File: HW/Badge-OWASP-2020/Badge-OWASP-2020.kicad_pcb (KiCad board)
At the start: 2 copper layers, 25 parts, among them J1 Conn_02x03_Odd_Even, J2 Screw_Terminal_01x04, J3 USB_B, Q1 MMBT3904, Q2 MMBT3904, SW1 RST, SW2 BOOT, U1 ESP32-WROOM-32, U2 CH340C, U3 AP111733

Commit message: define design :D
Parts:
- added J2: Battery, Connector_PinHeader_2.54mm:PinHeader_1x02_P2.54mm_Vertical, F.Cu at (163.3, 89.2)
- added Q2: DMG3415U-7, Package_TO_SOT_SMD:SOT-23, B.Cu at (147.6, 61.2)
- added R7: 100K, Resistor_SMD:R_0805_2012Metric_Pad1.15x1.40mm_HandSolder, B.Cu at (147.8, 56.9)
- added Ref**: Val**, Aesthetics:Badge_2020_OWASP, F.Cu at (147.1, 66.0)
- C1, C2, C3, C4, C5, D1, D2, D3, F1, Q1, R1, R2, R3, R4, R5, R6, U1, U2: moved to B.Cu
- J1: value Conn_02x03_Odd_Even -> Shitty Add-Ons; moved to B.Cu
- J3: renamed from J2; value Screw_Terminal_01x04 -> I2C
- J4: renamed from J3; moved to B.Cu
- Q3: renamed from Q2; moved to B.Cu
- U3: value AP111733 -> AP1117; moved to B.Cu
- moved D1 91.4 mm to (118.6, 71.1)
- moved R1 85.3 mm to (113.0, 51.3)
- moved C1 84.2 mm to (113.0, 47.2)
- moved D2 82.8 mm to (127.5, 81.8)
- moved J3 80.0 mm to (104.6, 36.3)
- moved R6 76.5 mm to (123.1, 57.2)
- moved Q3 74.2 mm to (127.7, 59.4)
- moved R2 73.4 mm to (123.1, 60.2)
- moved R5 69.6 mm to (130.1, 64.3)
- moved C3 67.7 mm to (140.8, 54.0)
- moved C4 67.7 mm to (140.0, 57.4)
- moved D3 67.7 mm to (135.7, 54.2)
- moved R4 67.7 mm to (140.0, 60.3)
- moved R3 67.4 mm to (130.1, 67.2)
- moved Q1 66.1 mm to (138.3, 69.4)
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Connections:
- D2 pad 2: Net-(D2-Pad2) -> /GPIO1
- J1 pad 1: GND -> +3V3
- J1 pad 2: +3V3 -> GND
- J1 pad 3: /SCL -> /SDA
- J1 pad 4: /SDA -> /SCL
- J1 pad 5: /GPIO2 -> /GPIO1
- J1 pad 6: /GPIO1 -> /GPIO2
- U1 pad 24: /GPIO1 -> Net-(U1-Pad24)
- U2 pad 2: /TXD -> /TX
- U2 pad 3: /RXD -> /RX
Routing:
- added copper zone on F.Cu, net GND
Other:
- board outline added: 98.6 x 65.9 mm

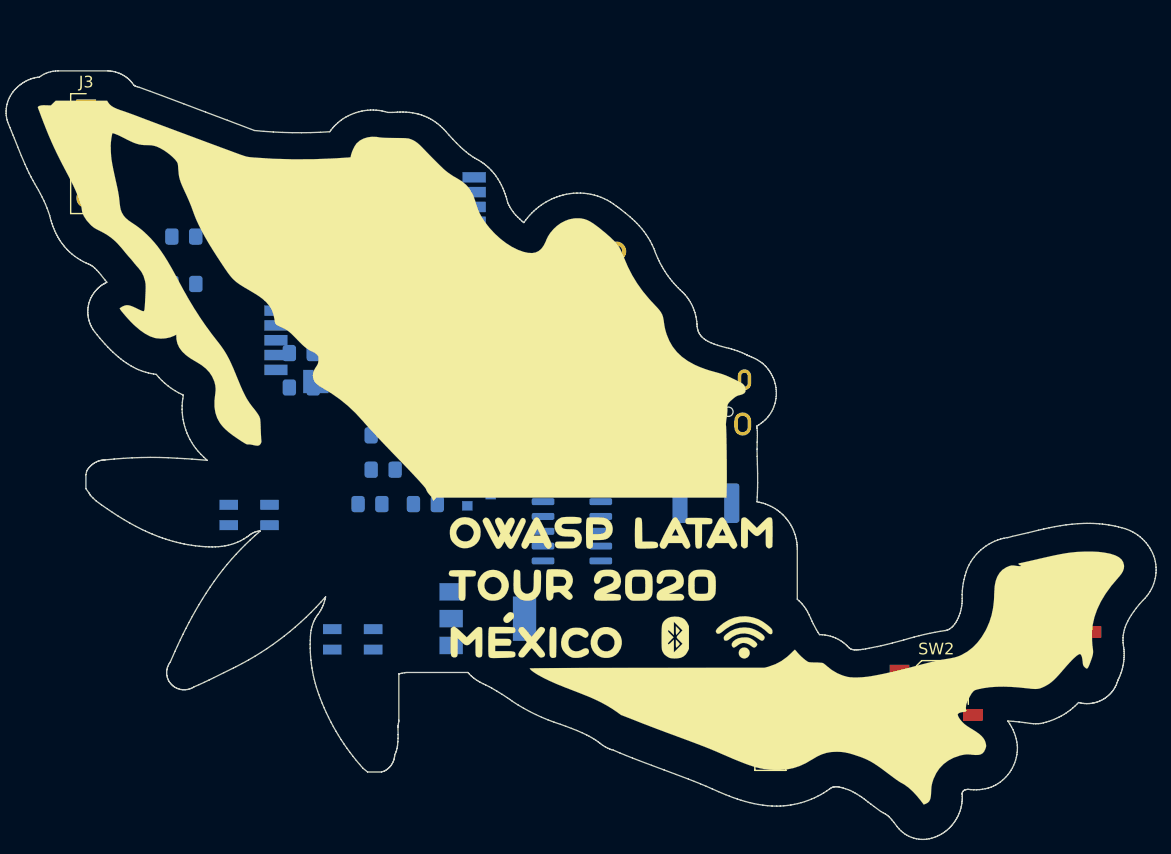
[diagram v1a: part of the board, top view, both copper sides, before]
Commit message: component distribution
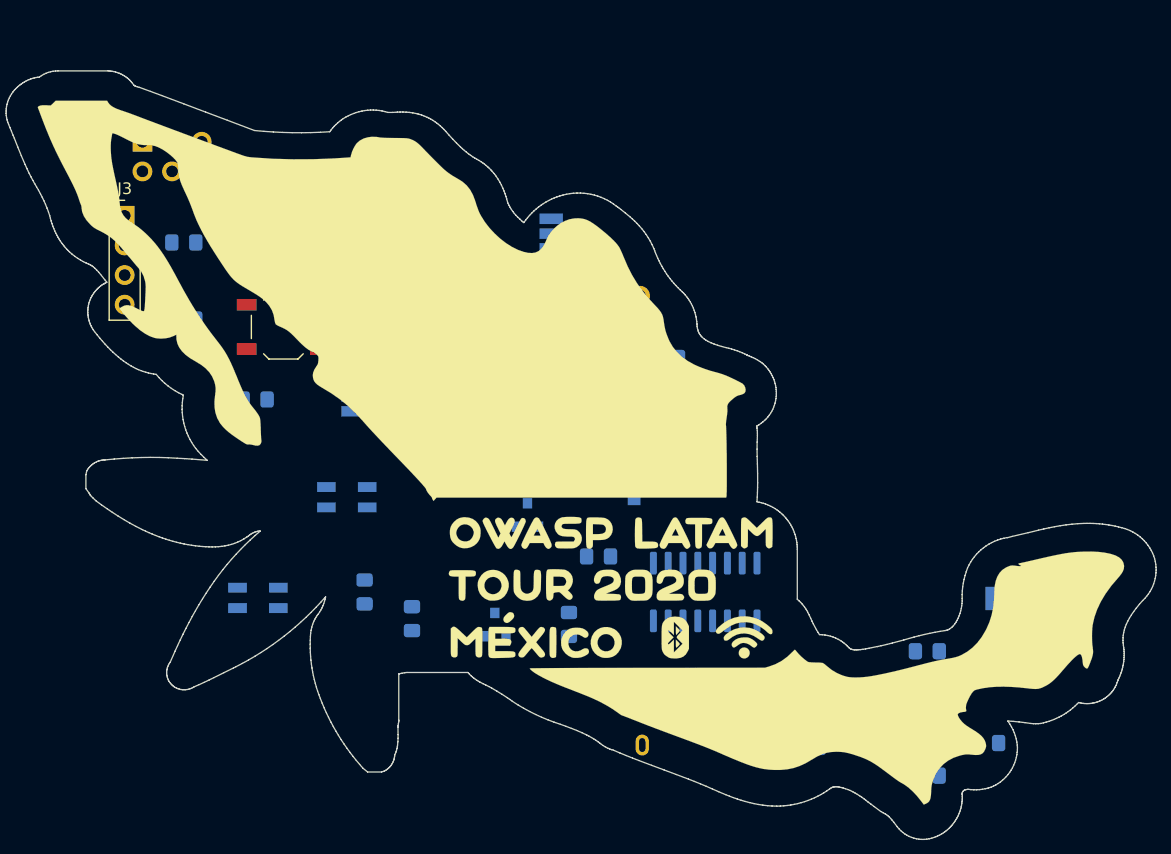
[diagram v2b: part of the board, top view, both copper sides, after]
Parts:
- J2: moved to B.Cu
- moved SW1 70.4 mm to (121.6, 55.0)
- moved SW2 68.1 mm to (121.5, 47.6)
- moved C4 53.5 mm to (181.9, 90.7)
- moved R7 46.6 mm to (176.8, 93.5)
- moved C5 44.9 mm to (176.8, 82.8)
- moved U3 44.6 mm to (183.7, 81.4), turned to 90 degrees
- moved R1 43.0 mm to (154.7, 62.0)
- moved C1 42.7 mm to (154.4, 57.7)
- moved J1 42.4 mm to (109.5, 39.1), turned to 270 degrees
- moved Q2 40.1 mm to (176.8, 88.6)
- moved J2 39.3 mm to (149.6, 52.3), turned to 270 degrees
- moved R6 32.7 mm to (146.1, 80.5), turned to 90 degrees
- moved R4 29.8 mm to (113.0, 47.8), turned to 180 degrees
- moved R2 29.3 mm to (148.6, 74.7)
- moved J4 27.5 mm to (156.2, 88.9), turned to 180 degrees
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
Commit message: countour circle
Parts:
- moved J2 37.9 mm to (168.1, 85.3)
- moved SW1 36.8 mm to (157.1, 64.4)
- moved SW2 30.2 mm to (146.7, 64.4)
- moved Q3 6.01 mm to (143.6, 85.1)
- moved R6 5.79 mm to (149.6, 85.1)
- moved F1 2.64 mm to (164.8, 91.0)
- moved U2 1.44 mm to (158.8, 78.7)
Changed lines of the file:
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@@
   (general
     (thickness 1.6)
-    (drawings 2)
+    (drawings 5)
     (tracks 0)
     (zones 0)
@@
   (page A4)
   (layers
-    (0 F.Cu signal)
-    (31 B.Cu signal)
+    (0 F.Cu signal hide)
+    (31 B.Cu signal hide)
     (32 B.Adhes user)
     (33 F.Adhes user)
     (34 B.Paste user)
     (35 F.Paste user)
-    (36 B.SilkS user)
+    (36 B.SilkS user hide)
     (37 F.SilkS user hide)
     (38 B.Mask user)
@@
   )
   (module Connector_PinHeader_2.54mm:PinHeader_1x02_P2.54mm_Vertical (layer B.Cu)
-    (at 149.606 52.324 270)
+    (at 168.148 85.344 270)
     (descr "Through hole straight pin header, 1x02, 2.54mm pitch, single row")
     (tags "Through hole pin header THT 1x02 2.54mm single row")
@@
   )
   (module Package_SO:SOIC-16_3.9x9.9mm_P1.27mm (layer B.Cu)
-    (at 157.734 77.724 90)
+    (at 158.75 78.74 90)
     (descr "SOIC, 16 Pin (JEDEC MS-012AC, https://www.analog.com/media/en/package-pcb-resources/package/pkg_pdf/soic_narrow-r/r_16.pdf), generated with kicad-footprint-generator ipc_gullwing_generator.py")
     (tags "SOIC SO")
@@
   )
   (module Button_Switch_SMD:SW_SPST_TL3342 (layer F.Cu)
-    (at 121.514 47.62)
+    (at 146.66 64.394)
     (descr "Low-profile SMD Tactile Switch, https://www.e-switch.com/system/asset/product_line/data_sheet/165/TL3342.pdf")
     (tags "SPST Tactile Switch")
@@
   )
   (module Button_Switch_SMD:SW_SPST_TL3342 (layer F.Cu)
-    (at 121.564 54.996)
+    (at 157.124 64.394)
     (descr "Low-profile SMD Tactile Switch, https://www.e-switch.com/system/asset/product_line/data_sheet/165/TL3342.pdf")
     (tags "SPST Tactile Switch")
@@
   )
   (module Resistor_SMD:R_0805_2012Metric_Pad1.15x1.40mm_HandSolder (layer B.Cu)
-    (at 146.05 80.509 90)
+    (at 149.606 85.081 90)
     (descr "Resistor SMD 0805 (2012 Metric), square (rectangular) end terminal, IPC_7351 nominal with elongated pad for handsoldering. (Body size source: https://docs.google.com/spreadsheets/d/1BsfQQcO9C6DZCsRaXUlFlo91Tg2WpOkGARC1WS5S8t0/edit?usp=sharing), generated with kicad-footprint-generator")
     (tags "resistor handsolder")
@@
   )
   (module Package_TO_SOT_SMD:SOT-23 (layer B.Cu)
-    (at 139.7 80.518 90)
+    (at 143.576 85.106 90)
     (descr "SOT-23, Standard")
     (tags SOT-23)
@@
   )
   (module Fuse:Fuse_1812_4532Metric_Pad1.30x3.40mm_HandSolder (layer B.Cu)
-    (at 166.37 88.839 90)
+    (at 164.846 90.993 90)
     (descr "Fuse SMD 1812 (4532 Metric), square (rectangular) end terminal, IPC_7351 nominal with elongated pad for handsoldering. (Body size source: https://www.nikhef.nl/pub/departments/mt/projects/detectorR_D/dtddice/ERJ2G.pdf), generated with kicad-footprint-generator")
     (tags "resistor handsolder")
@@
     )
   )
+  (gr_circle (center 103.124 37.989769) (end 105.156 36.719769) (layer Edge.Cuts) (width 0.05))
+  (dimension 4.792462 (width 0.15) (layer Dwgs.User)
+    (gr_text "4.792 mm" (at 198.912 76.343769 270) (layer Dwgs.User)
+      (effects (font (size 1 1) (thickness 0.15)))
+    )
+    (feature1 (pts (xy 191.77 78.74) (xy 198.198421 78.74)))
+    (feature2 (pts (xy 191.77 73.947538) (xy 198.198421 73.947538)))
+    (crossbar (pts (xy 197.612 73.947538) (xy 197.612 78.74)))
+    (arrow1a (pts (xy 197.612 78.74) (xy 197.025579 77.613496)))
+    (arrow1b (pts (xy 197.612 78.74) (xy 198.198421 77.613496)))
+    (arrow2a (pts (xy 197.612 73.947538) (xy 197.025579 75.074042)))
+    (arrow2b (pts (xy 197.612 73.947538) (xy 198.198421 75.074042)))
+  )
+  (gr_circle (center 191.77 76.343769) (end 193.802 75.073769) (layer Edge.Cuts) (width 0.05))
   (dimension 99.080164 (width 0.15) (layer Margin)
     (gr_text "99.080 mm" (at 148.26013 123.912709 0.1040899169) (layer Margin)

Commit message: logos space
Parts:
- moved C3 21.9 mm to (115.3, 82.8)
- moved R5 12.0 mm to (144.5, 80.8), turned to 0 degrees
- moved D3 6.55 mm to (157.9, 70.4), turned to 180 degrees
- moved Q1 5.18 mm to (144.3, 76.0)
- moved R2 4.75 mm to (149.9, 79.2), turned to 90 degrees
- moved R1 4.69 mm to (157.7, 65.5)
- moved C1 4.13 mm to (157.5, 60.5)
- moved C2 3.64 mm to (127.8, 74.2), turned to 0 degrees
- moved D2 0.84 mm to (119.9, 77.6)
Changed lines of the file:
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@@
   (page A4)
   (layers
-    (0 F.Cu signal hide)
-    (31 B.Cu signal hide)
+    (0 F.Cu signal)
+    (31 B.Cu signal)
     (32 B.Adhes user)
     (33 F.Adhes user)
     (34 B.Paste user)
     (35 F.Paste user)
-    (36 B.SilkS user hide)
+    (36 B.SilkS user)
     (37 F.SilkS user hide)
     (38 B.Mask user)
@@
   )
   (module Resistor_SMD:R_0805_2012Metric_Pad1.15x1.40mm_HandSolder (layer B.Cu)
-    (at 132.588 80.01 270)
+    (at 144.526 80.772)
     (descr "Resistor SMD 0805 (2012 Metric), square (rectangular) end terminal, IPC_7351 nominal with elongated pad for handsoldering. (Body size source: https://docs.google.com/spreadsheets/d/1BsfQQcO9C6DZCsRaXUlFlo91Tg2WpOkGARC1WS5S8t0/edit?usp=sharing), generated with kicad-footprint-generator")
     (tags "resistor handsolder")
     (attr smd)
-    (fp_text reference R5 (at 0 1.65 90) (layer B.SilkS)
+    (fp_text reference R5 (at 0 1.65) (layer B.SilkS)
       (effects (font (size 1 1) (thickness 0.15)) (justify mirror))
     )
-    (fp_text value 10K (at 0 -1.65 90) (layer B.Fab)
+    (fp_text value 10K (at 0 -1.65) (layer B.Fab)
       (effects (font (size 1 1) (thickness 0.15)) (justify mirror))
     )
-    (fp_text user %R (at 0 0 90) (layer B.Fab)
+    (fp_text user %R (at 0 0) (layer B.Fab)
       (effects (font (size 0.5 0.5) (thickness 0.08)) (justify mirror))
     )
@@
     (fp_line (start -1 0.6) (end 1 0.6) (layer B.Fab) (width 0.1))
     (fp_line (start -1 -0.6) (end -1 0.6) (layer B.Fab) (width 0.1))
-    (pad 2 smd roundrect (at 1.025 0 270) (size 1.15 1.4) (layers B.Cu B.Paste B.Mask) (roundrect_rratio 0.217391)
+    (pad 2 smd roundrect (at 1.025 0) (size 1.15 1.4) (layers B.Cu B.Paste B.Mask) (roundrect_rratio 0.217391)
       (net 17 /DTR))
-    (pad 1 smd roundrect (at -1.025 0 270) (size 1.15 1.4) (layers B.Cu B.Paste B.Mask) (roundrect_rratio 0.217391)
+    (pad 1 smd roundrect (at -1.025 0) (size 1.15 1.4) (layers B.Cu B.Paste B.Mask) (roundrect_rratio 0.217391)
       (net 16 "Net-(Q1-Pad1)"))
     (model ${KISYS3DMOD}/Resistor_SMD.3dshapes/R_0805_2012Metric.wrl
@@
   )
   (module Resistor_SMD:R_0805_2012Metric_Pad1.15x1.40mm_HandSolder (layer B.Cu)
-    (at 148.59 74.676)
+    (at 149.86 79.248 90)
     (descr "Resistor SMD 0805 (2012 Metric), square (rectangular) end terminal, IPC_7351 nominal with elongated pad for handsoldering. (Body size source: https://docs.google.com/spreadsheets/d/1BsfQQcO9C6DZCsRaXUlFlo91Tg2WpOkGARC1WS5S8t0/edit?usp=sharing), generated with kicad-footprint-generator")
     (tags "resistor handsolder")
     (attr smd)
-    (fp_text reference R2 (at 0 1.65) (layer B.SilkS)
+    (fp_text reference R2 (at 0 1.65 90) (layer B.SilkS)
       (effects (font (size 1 1) (thickness 0.15)) (justify mirror))
     )
-    (fp_text value 470 (at 0 -1.65) (layer B.Fab)
+    (fp_text value 470 (at 0 -1.65 90) (layer B.Fab)
       (effects (font (size 1 1) (thickness 0.15)) (justify mirror))
     )
-    (fp_text user %R (at 0 0) (layer B.Fab)
+    (fp_text user %R (at 0 0 90) (layer B.Fab)
       (effects (font (size 0.5 0.5) (thickness 0.08)) (justify mirror))
     )
@@
     (fp_line (start -1 0.6) (end 1 0.6) (layer B.Fab) (width 0.1))
     (fp_line (start -1 -0.6) (end -1 0.6) (layer B.Fab) (width 0.1))
-    (pad 2 smd roundrect (at 1.025 0) (size 1.15 1.4) (layers B.Cu B.Paste B.Mask) (roundrect_rratio 0.217391)
+    (pad 2 smd roundrect (at 1.025 0 90) (size 1.15 1.4) (layers B.Cu B.Paste B.Mask) (roundrect_rratio 0.217391)
       (net 19 "Net-(R2-Pad2)"))
-    (pad 1 smd roundrect (at -1.025 0) (size 1.15 1.4) (layers B.Cu B.Paste B.Mask) (roundrect_rratio 0.217391)
+    (pad 1 smd roundrect (at -1.025 0 90) (size 1.15 1.4) (layers B.Cu B.Paste B.Mask) (roundrect_rratio 0.217391)
       (net 5 /NP))
     (model ${KISYS3DMOD}/Resistor_SMD.3dshapes/R_0805_2012Metric.wrl
@@
   )
   (module Resistor_SMD:R_0805_2012Metric_Pad1.15x1.40mm_HandSolder (layer B.Cu)
-    (at 154.677 61.976)
+    (at 157.734 65.532)
     (descr "Resistor SMD 0805 (2012 Metric), square (rectangular) end terminal, IPC_7351 nominal with elongated pad for handsoldering. (Body size source: https://docs.google.com/spreadsheets/d/1BsfQQcO9C6DZCsRaXUlFlo91Tg2WpOkGARC1WS5S8t0/edit?usp=sharing), generated with kicad-footprint-generator")
     (tags "resistor handsolder")
@@
   )
   (module Package_TO_SOT_SMD:SOT-23 (layer B.Cu)
-    (at 142.494 71.12 90)
+    (at 144.338 75.962 90)
     (descr "SOT-23, Standard")
     (tags SOT-23)
@@
   )
   (module Diode_SMD:D_SOD-123F (layer B.Cu)
-    (at 151.638 68.326 270)
+    (at 157.864 70.358 180)
     (descr D_SOD-123F)
     (tags D_SOD-123F)
     (attr smd)
-    (fp_text reference D3 (at -0.127 1.905 90) (layer B.SilkS)
+    (fp_text reference D3 (at -0.127 1.905) (layer B.SilkS)
       (effects (font (size 1 1) (thickness 0.15)) (justify mirror))
     )
-    (fp_text value MBR120 (at 0 -2.1 90) (layer B.Fab)
+    (fp_text value MBR120 (at 0 -2.1) (layer B.Fab)
       (effects (font (size 1 1) (thickness 0.15)) (justify mirror))
     )
@@
     (fp_line (start 0.25 0) (end 0.75 0) (layer B.Fab) (width 0.1))
     (fp_line (start -2.2 1) (end -2.2 -1) (layer B.SilkS) (width 0.12))
-    (fp_text user %R (at -0.127 1.905 90) (layer B.Fab)
+    (fp_text user %R (at -0.127 1.905) (layer B.Fab)
       (effects (font (size 1 1) (thickness 0.15)) (justify mirror))
     )
-    (pad 2 smd rect (at 1.4 0 270) (size 1.1 1.1) (layers B.Cu B.Paste B.Mask)
+    (pad 2 smd rect (at 1.4 0 180) (size 1.1 1.1) (layers B.Cu B.Paste B.Mask)
       (net 6 VCC))
-    (pad 1 smd rect (at -1.4 0 270) (size 1.1 1.1) (layers B.Cu B.Paste B.Mask)
+    (pad 1 smd rect (at -1.4 0 180) (size 1.1 1.1) (layers B.Cu B.Paste B.Mask)
       (net 3 "Net-(C5-Pad1)"))
     (model ${KISYS3DMOD}/Diode_SMD.3dshapes/D_SOD-123F.wrl
@@
   )
   (module LED_SMD:LED_SK6812MINI_PLCC4_3.5x3.5mm_P1.75mm (layer B.Cu)
-    (at 119.38 78.232)
+    (at 119.916 77.583)
     (descr https://cdn-shop.adafruit.com/product-files/2686/SK6812MINI_REV.01-1-2.pdf)
     (tags "LED RGB NeoPixel Mini")
@@
   )
   (module Capacitor_SMD:C_0805_2012Metric_Pad1.15x1.40mm_HandSolder (layer B.Cu)
-    (at 119.135 61.214)
+    (at 115.316 82.804)
     (descr "Capacitor SMD 0805 (2012 Metric), square (rectangular) end terminal, IPC_7351 nominal with elongated pad for handsoldering. (Body size source: https://docs.google.com/spreadsheets/d/1BsfQQcO9C6DZCsRaXUlFlo91Tg2WpOkGARC1WS5S8t0/edit?usp=sharing), generated with kicad-footprint-generator")
     (tags "capacitor handsolder")
@@
   )
   (module Capacitor_SMD:C_0805_2012Metric_Pad1.15x1.40mm_HandSolder (layer B.Cu)
-    (at 128.524 77.724 90)
+    (at 127.753 74.168)
     (descr "Capacitor SMD 0805 (2012 Metric), square (rectangular) end terminal, IPC_7351 nominal with elongated pad for handsoldering. (Body size source: https://docs.google.com/spreadsheets/d/1BsfQQcO9C6DZCsRaXUlFlo91Tg2WpOkGARC1WS5S8t0/edit?usp=sharing), generated with kicad-footprint-generator")
     (tags "capacitor handsolder")
     (attr smd)
-    (fp_text reference C2 (at 0 1.65 90) (layer B.SilkS)
+    (fp_text reference C2 (at 0 1.65) (layer B.SilkS)
       (effects (font (size 1 1) (thickness 0.15)) (justify mirror))
     )
-    (fp_text value 0.1uF (at 0 -1.65 90) (layer B.Fab)
+    (fp_text value 0.1uF (at 0 -1.65) (layer B.Fab)
       (effects (font (size 1 1) (thickness 0.15)) (justify mirror))
     )
-    (fp_text user %R (at 0 0 90) (layer B.Fab)
+    (fp_text user %R (at 0 0) (layer B.Fab)
       (effects (font (size 0.5 0.5) (thickness 0.08)) (justify mirror))
     )
@@
     (fp_line (start -1 0.6) (end 1 0.6) (layer B.Fab) (width 0.1))
     (fp_line (start -1 -0.6) (end -1 0.6) (layer B.Fab) (width 0.1))
-    (pad 2 smd roundrect (at 1.025 0 90) (size 1.15 1.4) (layers B.Cu B.Paste B.Mask) (roundrect_rratio 0.217391)
+    (pad 2 smd roundrect (at 1.025 0) (size 1.15 1.4) (layers B.Cu B.Paste B.Mask) (roundrect_rratio 0.217391)
       (net 1 GND))
-    (pad 1 smd roundrect (at -1.025 0 90) (size 1.15 1.4) (layers B.Cu B.Paste B.Mask) (roundrect_rratio 0.217391)
+    (pad 1 smd roundrect (at -1.025 0) (size 1.15 1.4) (layers B.Cu B.Paste B.Mask) (roundrect_rratio 0.217391)
       (net 2 +3V3))
     (model ${KISYS3DMOD}/Capacitor_SMD.3dshapes/C_0805_2012Metric.wrl
@@
   )
   (module Capacitor_SMD:C_0805_2012Metric_Pad1.15x1.40mm_HandSolder (layer B.Cu)
-    (at 154.423 57.658)
+    (at 157.471 60.452)
     (descr "Capacitor SMD 0805 (2012 Metric), square (rectangular) end terminal, IPC_7351 nominal with elongated pad for handsoldering. (Body size source: https://docs.google.com/spreadsheets/d/1BsfQQcO9C6DZCsRaXUlFlo91Tg2WpOkGARC1WS5S8t0/edit?usp=sharing), generated with kicad-footprint-generator")
     (tags "capacitor handsolder")

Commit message: add logos
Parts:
- added G***: LOGO, Aesthetics:espressif, B.Cu at (147.1, 73.4)
- added G***: LOGO, Aesthetics:lcsc, B.Cu at (159.5, 77.7)
- added G***: LOGO, Aesthetics:pcbway_13x4, B.Cu at (145.0, 81.8)
- added G***: LOGO, Aesthetics:electronic_cats_logo_8x6, B.Cu at (135.9, 77.2)
